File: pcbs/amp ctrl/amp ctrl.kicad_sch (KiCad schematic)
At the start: 60 parts, among them J1 Conn_02x25_Odd_Even, J13 Conn_02x02, J4 Conn_01x02, U10 ADA4004-1, U70 MCP1754ST-3302

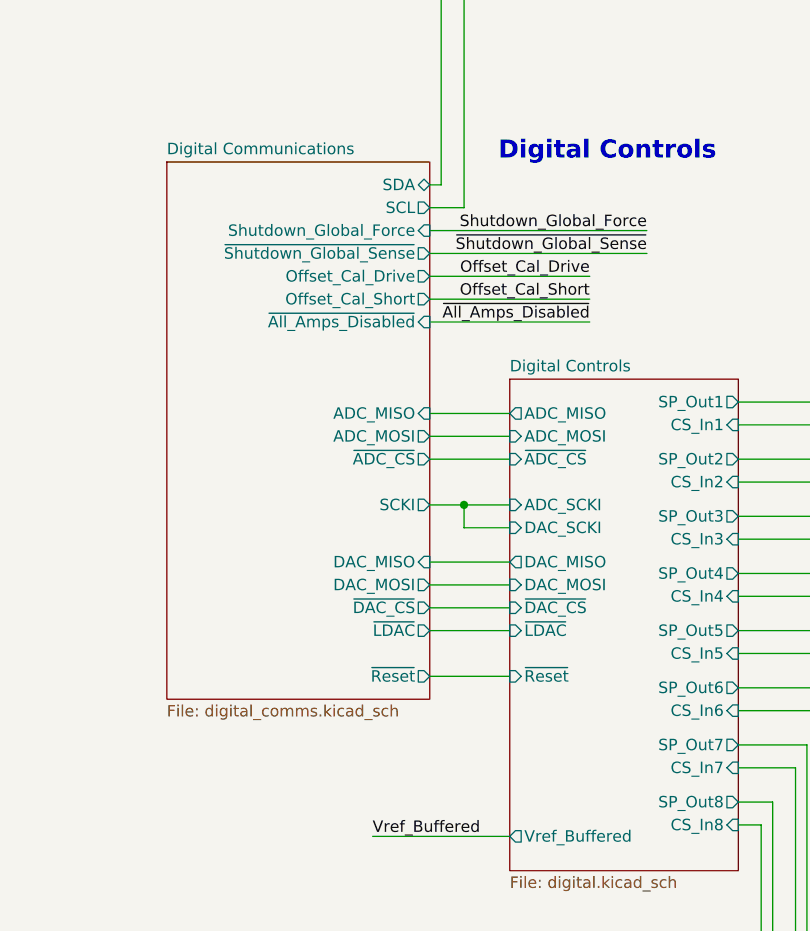
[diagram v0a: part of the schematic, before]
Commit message: Backplane comms updates, manufacturing renaming
Removed misspelled "maunfacturing" folder, fixed gitignore rule to remove manufacturing folders within individual PCB folders too
Changed SCKI/SCKO terminology to SCK, SCK_LB (loopback) for clarity
Added ADC_CS loopback signal between amp ctrl board & backplane for better fast-clock timing (#38)
Backplane: changed LVDS FPGA outputs to single-ended FPGA outputs to gain more I/O pins, added external LVDS transceivers (#38)
Backplane: replaced global clock & ~LDAC buffers with a separate FPGA pin for each amp ctrl board (#38)
Backplane: removed +2.5V power supply and level translations, no longer needed without FPGA I/O pins using LVDS_25 I/O configuration
Backplane: replaced +VDC-input resistor with solder jumper (on by default)
Backplane: changed field names (Part Number to MPN) to match Aisler's naming convention for automatic recognition
Amp ctrl: fixed optional level-shifter circuit on each channel for voltage inputs (#9) schematic & channel-1 layout
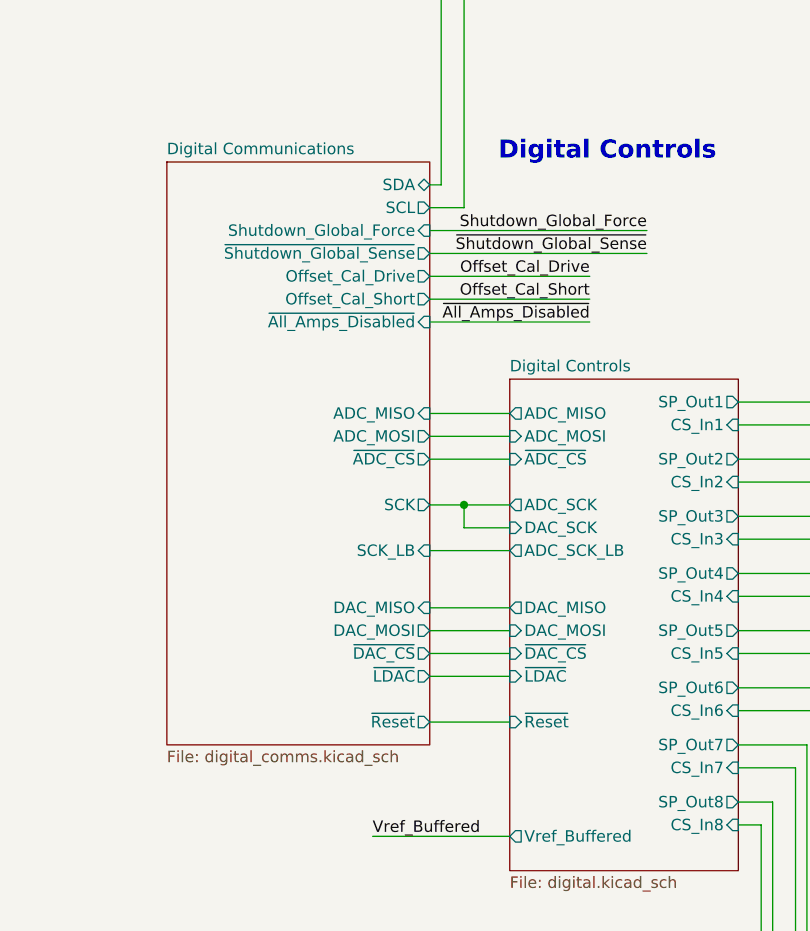
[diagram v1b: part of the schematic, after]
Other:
- sheet Digital Communications ports: added SCK, SCK_LB; removed SCKI
- sheet Digital Controls ports: added ADC_SCK, ADC_SCK_LB, DAC_SCK; removed ADC_SCKI, DAC_SCKI
